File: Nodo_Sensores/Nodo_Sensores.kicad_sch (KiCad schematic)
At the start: 1 part, among them U1 ESP-12F

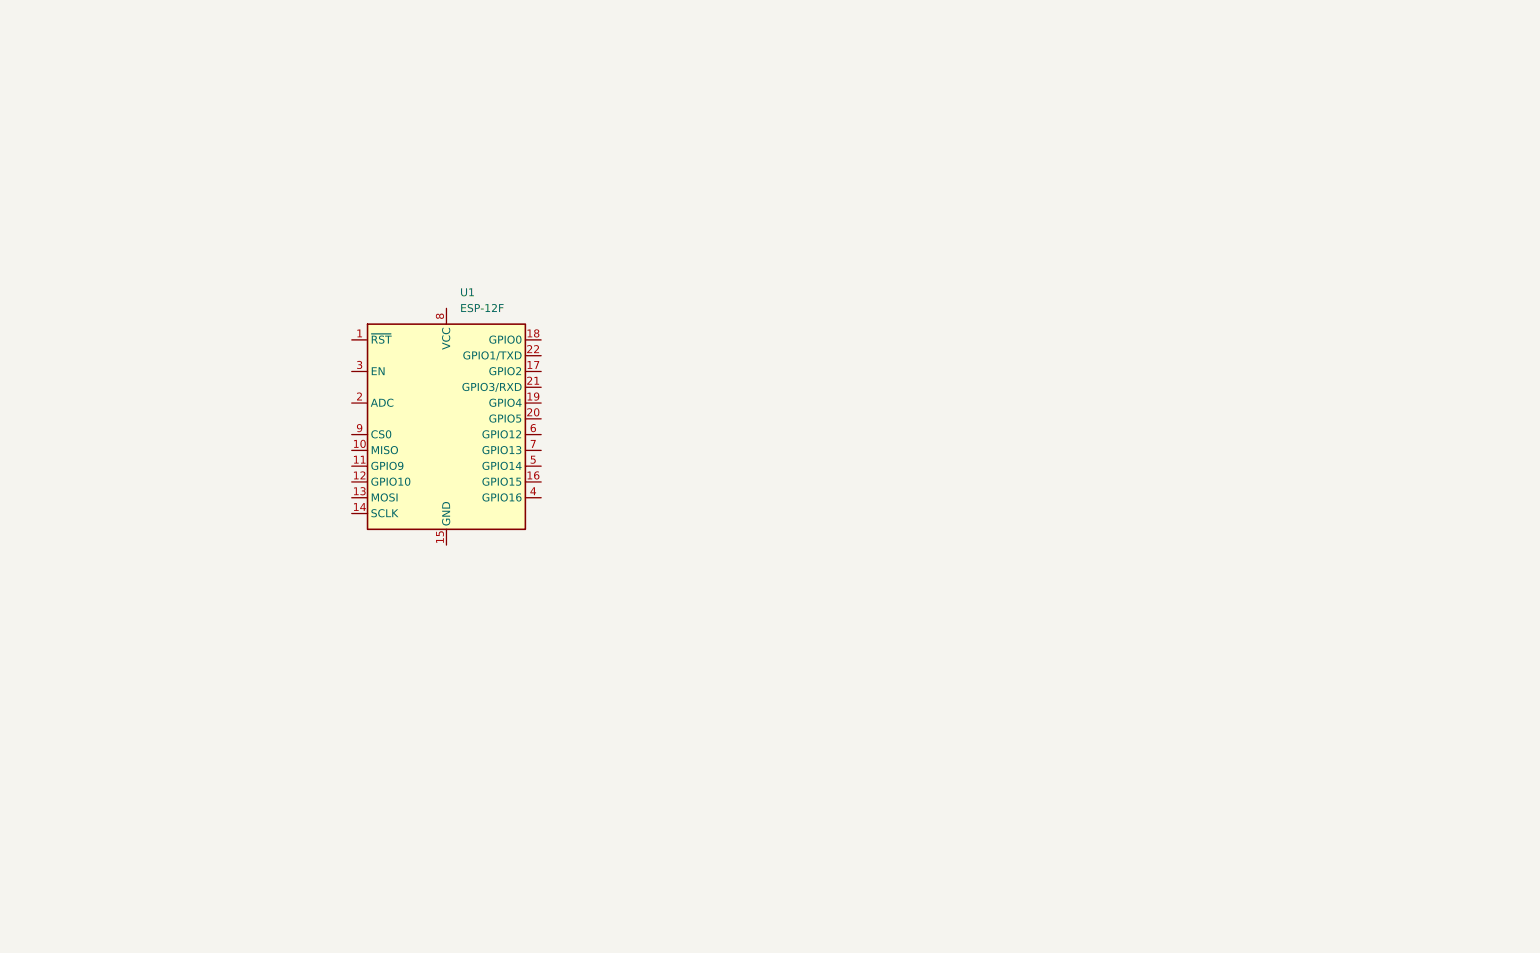
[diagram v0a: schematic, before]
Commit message: Se avanzó con el esquematico. Falta definir método de prog del esp y agregar protecciones
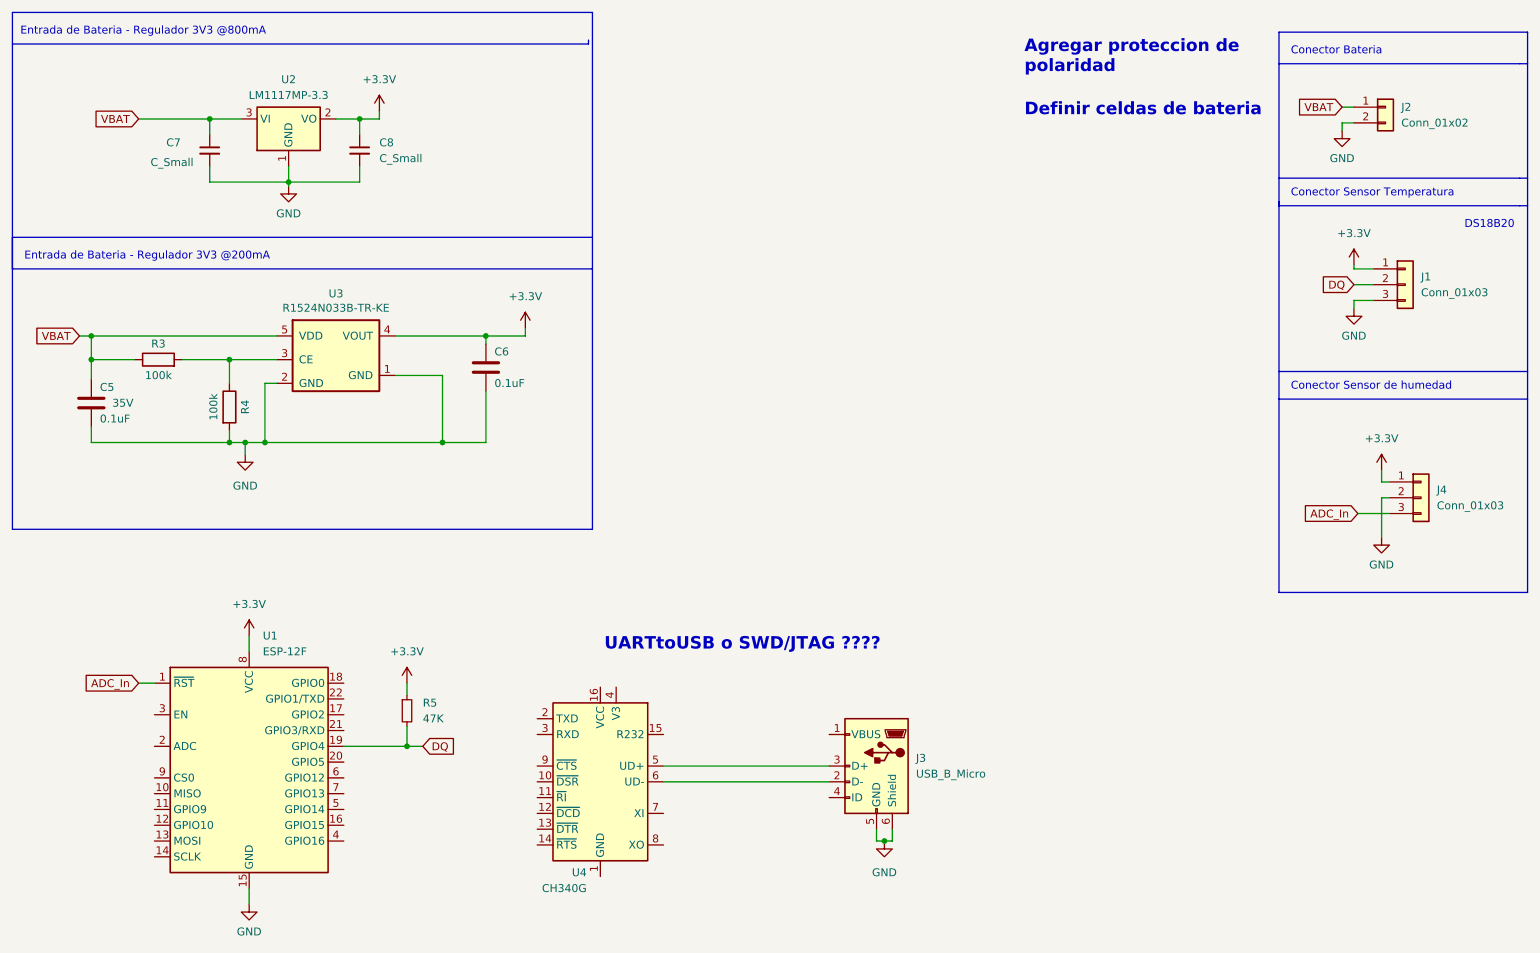
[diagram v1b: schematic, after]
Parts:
- added C5: 0.1uF, Capacitor_SMD:C_0805_2012Metric, symbol Device:C
- added C6: 0.1uF, Capacitor_SMD:C_0603_1608Metric, symbol Device:C
- added C7, C8: C_Small, symbol Device:C_Small
- added J1, J4: Conn_01x03, symbol Connector_Generic:Conn_01x03
- added J2: Conn_01x02, symbol Connector_Generic:Conn_01x02
- added J3: USB_B_Micro, symbol Connector:USB_B_Micro
- added R3, R4: 100k, Resistor_SMD:R_0805_2012Metric_Pad1.20x1.40mm_HandSolder, symbol Device:R
- added R5: 47K, Resistor_SMD:R_0805_2012Metric_Pad1.20x1.40mm_HandSolder, symbol Device:R_Small
- added U2: LM1117MP-3.3, Package_TO_SOT_SMD:SOT-223-3_TabPin2, symbol Regulator_Linear:LM1117MP-3.3
- added U3: R1524N033B-TR-KE, Package_TO_SOT_SMD:SOT-23-5, symbol R1524N033B:R1524N033B
- added U4: CH340G, Package_SO:SOIC-16_3.9x9.9mm_P1.27mm, symbol Interface_USB:CH340G
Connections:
- net ADC_In: now reaches U1.1 (~{RST})
- net ADC_In: now also J4.3 (Pin_3)
- net GND: now reaches U1.15 (GND)
- net GND: now also C5.1, C6.1, C7.2, C8.2, J1.3 (Pin_3), J2.2 (Pin_2), J3.5 (GND), J3.6 (Shield), J4.2 (Pin_2), R4.2, U2.1 (GND), U3.1 (GND), U3.2 (GND)
- net DQ: now reaches U1.19 (GPIO4)
- net DQ: now also J1.2 (Pin_2), R5.2
- net +3.3V: now reaches U1.8 (VCC)
- net +3.3V: now also C6.2, C8.1, J1.1 (Pin_1), J4.1 (Pin_1), R5.1, U2.2 (VO), U3.4 (VOUT)
- new net: R3.2, R4.1, U3.3 (CE)
- new net: J3.2 (D-), U4.6 (UD-)
- new net: J3.3 (D+), U4.5 (UD+)
- new net VBAT: C5.2, C7.1, J2.1 (Pin_1), R3.1, U2.3 (VI), U3.5 (VDD)
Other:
- note added: "Conector Bateria"
- note added: "Conector Sensor Temperatura"
- note added: "Conector Sensor de humedad"
- note added: "DS18B20"
- note added: "Entrada de Bateria - Regulador 3V3 @200mA"
- note added: "Entrada de Bateria - Regulador 3V3 @800mA"
- note added: "UARTtoUSB o SWD/JTAG ????"
- moved on the sheet: U1

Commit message: modificacion sch
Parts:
- removed C5: 0.1uF, Capacitor_SMD:C_0805_2012Metric, symbol Device:C
- removed C6: 0.1uF, Capacitor_SMD:C_0603_1608Metric, symbol Device:C
- removed C7, C8: C_Small, symbol Device:C_Small
- removed J3: USB_B_Micro, symbol Connector:USB_B_Micro
- removed R5: 47K, Resistor_SMD:R_0805_2012Metric_Pad1.20x1.40mm_HandSolder, symbol Device:R_Small
- removed U4: CH340G, Package_SO:SOIC-16_3.9x9.9mm_P1.27mm, symbol Interface_USB:CH340G
- added C5, C6: C_Small, symbol Device:C_Small
- added C7: 0.1uF, Capacitor_SMD:C_0603_1608Metric, symbol Device:C
- added C8: 0.1uF, Capacitor_SMD:C_0805_2012Metric, symbol Device:C
- added J3: Conn_01x05, Connector_PinHeader_2.54mm:PinHeader_1x05_P2.54mm_Vertical, symbol Connector_Generic:Conn_01x05
- added R1: 47K, Resistor_SMD:R_0805_2012Metric_Pad1.20x1.40mm_HandSolder, symbol Device:R
- added R2, R5, R6, R7: 10K, Resistor_SMD:R_0805_2012Metric_Pad1.20x1.40mm_HandSolder, symbol Device:R
- added U4: TS3702, Package_SO:SOIC-8-1EP_3.9x4.9mm_P1.27mm_EP2.514x3.2mm, symbol Comparator:LM393
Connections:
- net +3.3V: now also C6.1, C7.2, R1.1, R2.1, R5.1, R7.1, U4.8 (V+)
- net ADC_In: now also U1.2 (ADC); no longer U1.1 (~{RST})
- net DQ: now also R1.2
- net GND: now also C5.2, C6.2, C7.1, C8.1, J3.1 (Pin_1), R6.2, U4.4 (V-)
- net VBAT: now also C5.1, C8.2
- net at U1.16 (GPIO15): now also R6.1
- net DTR: now reaches U1.18 (GPIO0)
- net DTR: now also J3.5 (Pin_5), R7.2
- net ESP_RX: now reaches U1.21 (GPIO3/RXD)
- net ESP_RX: now also J3.3 (Pin_3)
- net ESP_TX: now reaches U1.22 (GPIO1/TXD)
- net ESP_TX: now also J3.4 (Pin_4)
- net at U1.3 (EN): now also R5.2
- new net RTS: J3.2 (Pin_2), R2.2, U1.1 (~{RST})
- no-connect marks 0 -> 3
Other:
- added sheet StepDown_Vbat_to_3V3 (untitled.kicad_sch)
- note added: "Comparador (Porque en el esp12F tengo el adc ocupado)"
- note added: "Conector Programador"
- note added: "ESP12F"
- note added: "Entrada de Bateria - Regulador 3V3 @200mA max"
- note added: "Entrada de Bateria - Regulador 3V3 @800mA max"
- note removed: "Entrada de Bateria - Regulador 3V3 @200mA"
- note removed: "Entrada de Bateria - Regulador 3V3 @800mA"
- note removed: "UARTtoUSB o SWD/JTAG ????"
- moved on the sheet: U1

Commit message: Nodo_Sensores V1.0
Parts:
- removed C5, C6: C_Small, symbol Device:C_Small
- removed C8: 0.1uF, Capacitor_SMD:C_0805_2012Metric, symbol Device:C
- removed U2: LM1117MP-3.3, Package_TO_SOT_SMD:SOT-223-3_TabPin2, symbol Regulator_Linear:LM1117MP-3.3
- removed U3: R1524N033B-TR-KE, Package_TO_SOT_SMD:SOT-23-5, symbol R1524N033B:R1524N033B
- removed U4: TS3702, Package_SO:SOIC-8-1EP_3.9x4.9mm_P1.27mm_EP2.514x3.2mm, symbol Comparator:LM393
- added C1: 100nF, Capacitor_SMD:C_1206_3216Metric, symbol Device:C
- added C10, C11, C4, C9: 22uF, Capacitor_SMD:C_1210_3225Metric, symbol Device:C
- added C12: 1uF, Capacitor_SMD:C_0805_2012Metric, symbol Device:C
- added C2: 10uF, Capacitor_SMD:C_1210_3225Metric, symbol Device:C
- added C3: 220nF, Capacitor_SMD:C_0805_2012Metric, symbol Device:C
- added C5, C6: 0.1uF, Capacitor_SMD:C_0805_2012Metric, symbol Device:C
- added D1: SK34A, Diode_SMD:D_SMA, symbol Diode:1N5819WS
- added D2: D, Diode_SMD:D_SMA, symbol Device:D
- added L1: 6.8uH, Inductor_SMD:L_12x12mm_H8mm, symbol Device:L_Ferrite
- added R10: 43,2K, Resistor_SMD:R_0805_2012Metric_Pad1.20x1.40mm_HandSolder, symbol Device:R
- added R11, R12, R14: 10k, Resistor_SMD:R_0805_2012Metric_Pad1.20x1.40mm_HandSolder, symbol Device:R
- added R13: 20k, Resistor_SMD:R_0805_2012Metric_Pad1.20x1.40mm_HandSolder, symbol Device:R
- added R8, R9: 100k, Resistor_SMD:R_0805_2012Metric_Pad1.20x1.40mm_HandSolder, symbol Device:R
- added U2: R1524N033B-TR-KE, Package_TO_SOT_SMD:SOT-23-5, symbol R1524N033B:R1524N033B
- added U3: TS3702, Package_SO:SOIC-8-1EP_3.9x4.9mm_P1.27mm_EP2.514x3.2mm, symbol Comparator:LM393
- added U5: LMR33630ADDA, Package_SO:Texas_HSOP-8-1EP_3.9x4.9mm_P1.27mm_ThermalVias, symbol Regulator_Switching:LMR33630ADDA
- C7: footprint Capacitor_SMD:C_0603_1608Metric -> Capacitor_SMD:C_0805_2012Metric
- J1, J4: footprint (none) -> Connector_Molex:Molex_KK-254_AE-6410-03A_1x03_P2.54mm_Vertical
- J2: footprint (none) -> Connector_Phoenix_MC:PhoenixContact_MCV_1,5_2-G-3.5_1x02_P3.50mm_Vertical
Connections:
- net +3.3V: now also C7.1, C5.2, R11.1, U2.4 (VOUT), U3.8 (V+); no longer C7.2, J4.1 (Pin_1)
- net GND: now also C7.2, C10.2, C11.2, C12.2, C2.2, C3.2, C4.2, C5.1, C6.1, C9.2, D2.2 (A), R10.1, R12.2, R14.2, U2.1 (GND), U2.2 (GND), U3.4 (V-), U5.1 (PGND), U5.9 (AGND); no longer C7.1
- net at R3.2, R4.1: now also U2.3 (CE)
- net LOW_BAT: now reaches U1.6 (GPIO12)
- net LOW_BAT: now also U3.1
- net VBAT renamed +5V
- net +5V: now also J4.1 (Pin_1), C10.1, C11.1, C4.1, C6.2, C9.1, L1.2, R8.2, U2.5 (VDD); no longer J2.1 (Pin_1)
- new net: C2.1, C3.1, D1.1 (K), D2.1 (K), U5.2 (VIN), U5.3 (EN)
- new net: R12.1, R13.2, U3.2 (-)
- new net: R9.1, U5.4 (PG)
- new net: C12.1, R9.2, U5.6 (VCC)
- new net: C1.1, U5.7 (BOOT)
- new net: R11.2, R14.1, U3.3 (+)
- new net FB: R10.2, R8.1, U5.5 (FB)
- new net SW: C1.2, L1.1, U5.8 (SW)
- new net V_BAT: D1.2 (A), J2.1 (Pin_1), R13.1
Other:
- removed sheet StepDown_Vbat_to_3V3
- note added: "Detector de baja bateria"
- note added: "Fuente tipo step-down. Vin:3,8V a 36V. F=400Khz Rendimiento>95%"
- note added: "Regulador 5V a 3.3V"
- note added: "Valores de resistores indicados por hoja de dato del fabricante"
- note removed: "Comparador (Porque en el esp12F tengo el adc ocupado)"
- note removed: "Entrada de Bateria - Regulador 3V3 @200mA max"
- note removed: "Entrada de Bateria - Regulador 3V3 @800mA max"
- moved on the sheet: J1, J2, J3, J4, R1, R2, R5, R6, R7, U1
